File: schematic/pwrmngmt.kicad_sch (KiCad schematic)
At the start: 46 parts, among them U10 BSD316, U11 BSD316, U12 PC817, U13 PC817, U14 PC817, U15 AS431, U16 LM324, U17 XL6009, U18 PAM2305CGFADJ, U9 BSD316

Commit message: a
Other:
- title: (none) -> Power Managment
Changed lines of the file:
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@@
 (kicad_sch (version 20211123) (generator eeschema)
   (paper "A4")
+  (title_block
+    (title "Power Managment")
+    (date "2022-03-18")
+    (comment 1 "Engineer/Draftsman: Joesphan Lu")
+  )
   (junction (at 251.46 24.13) (diameter 0) (color 0 0 0 0)
   )

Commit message: e
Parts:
- removed C16: 100uF, Capacitor_SMD:C_1210_3225Metric_Pad1.33x2.70mm_HandSolder, symbol Device:C
- removed C17: 10uF, Capacitor_SMD:C_0805_2012Metric_Pad1.18x1.45mm_HandSolder, symbol Device:C
- removed C18: 1uF, Capacitor_SMD:C_0805_2012Metric_Pad1.18x1.45mm_HandSolder, symbol Device:C
- removed C20: Cfw (DNP), Capacitor_SMD:C_0805_2012Metric_Pad1.18x1.45mm_HandSolder, symbol Device:C
- removed L2: 10uH NR8040T100M, Inductor_SMD:L_Taiyo-Yuden_NR-80xx_HandSoldering, symbol Device:L
- removed R13: 33k, Resistor_SMD:R_0805_2012Metric_Pad1.20x1.40mm_HandSolder, symbol Device:R
- removed R14: 7.5k, Resistor_SMD:R_0805_2012Metric_Pad1.20x1.40mm_HandSolder, symbol Device:R
- removed R35, R36: 1k, Resistor_SMD:R_0805_2012Metric_Pad1.20x1.40mm_HandSolder, symbol Device:R
- removed R37, R38: 12.5k, Resistor_SMD:R_0805_2012Metric_Pad1.20x1.40mm_HandSolder, symbol Device:R
- removed unit 1 of U16
- removed U18: PAM2305CGFADJ, Package_DFN_QFN:DFN-6-1EP_2x2mm_P0.65mm_EP1x1.6mm, symbol Regulator_Switching:PAM2305CGFADJ
- added C?: 100nF, Capacitor_SMD:C_0805_2012Metric_Pad1.18x1.45mm_HandSolder, symbol Device:C
- added C?: 84nF, Capacitor_SMD:C_0805_2012Metric_Pad1.18x1.45mm_HandSolder, symbol Device:C
- added C? (x2): 1uF, Capacitor_SMD:C_0805_2012Metric_Pad1.18x1.45mm_HandSolder, symbol Device:C
- added C?: 10uF, Capacitor_SMD:C_0805_2012Metric_Pad1.18x1.45mm_HandSolder, symbol Device:C
- added C?: 100uF, Capacitor_SMD:C_1210_3225Metric_Pad1.33x2.70mm_HandSolder, symbol Device:C
- added L?: 33uH, Inductor_SMD:L_10.4x10.4_H4.8, symbol Device:L
- added R4: .1, Resistor_SMD:R_1206_3216Metric_Pad1.30x1.75mm_HandSolder, symbol Device:R
- added R5, R6: 1k, Resistor_SMD:R_0805_2012Metric_Pad1.20x1.40mm_HandSolder, symbol Device:R
- added R7: 12.5k, Resistor_SMD:R_0805_2012Metric_Pad1.20x1.40mm_HandSolder, symbol Device:R
- added R? (x2): 50k, Resistor_SMD:R_0805_2012Metric_Pad1.20x1.40mm_HandSolder, symbol Device:R
- added R?: 3k, Resistor_SMD:R_0805_2012Metric_Pad1.20x1.40mm_HandSolder, symbol Device:R
- added R?: 39k, Resistor_SMD:R_0805_2012Metric_Pad1.20x1.40mm_HandSolder, symbol Device:R
- added R?: 7.5k, Resistor_SMD:R_0805_2012Metric_Pad1.20x1.40mm_HandSolder, symbol Device:R
- added R?: 33k, Resistor_SMD:R_0805_2012Metric_Pad1.20x1.40mm_HandSolder, symbol Device:R
- added U5: LM324, Package_SO:SOIC-14_3.9x8.7mm_P1.27mm, symbol Amplifier_Operational:LM324
- added U?: AOZ6662DI, 1KicadLib:DFN_8_3x3mm_EP_1.25x2.7mm, symbol 1KicadLib:AOZ6662DI
- added U?: AS431, Package_TO_SOT_SMD:SOT-23_Handsoldering, symbol 1KicadLib:AS431
- D4: footprint Diode_SMD:D_SMC_Handsoldering -> Diode_SMD:D_SMA_Handsoldering
- L3: footprint Inductor_SMD:L_12x12mm_H4.5mm -> Inductor_SMD:L_10.4x10.4_H4.8
- R34: value .1 -> 12.5k; footprint Resistor_SMD:R_1206_3216Metric_Pad1.30x1.75mm_HandSolder -> Resistor_SMD:R_0805_2012Metric_Pad1.20x1.40mm_HandSolder
- U12, U13, U14: footprint Package_SO:SOP-4_3.8x4.1mm_P2.54mm -> Package_DIP:DIP-4_W7.62mm
- U15: footprint Package_TO_SOT_SMD:SOT-23-5_HandSoldering -> Package_TO_SOT_SMD:SOT-23_Handsoldering
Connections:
- net +3V3: now also C?.1, C?.1, C?.1, L?.2, R?.1
- net +BATT: now also R?.2
- net GND: now also U17.1 (GND), C?.2, C?.2, C?.2, C?.2, C?.2, R4.1, R6.2, R7.2, R?.2, U?.1 (GND), U?.9 (EP/GND); no longer BT3.2 (-), R34.2, U11.4 (S)
- net at R34.1: now also R6.1, U5.3 (+); no longer U17.1 (GND)
- net at U17.5 (FB): now also R34.2, U5.1
- new net: BT3.2 (-), R4.2, R5.2, U11.4 (S)
- new net: C?.1, U?.8 (BOOTSTRP)
- new net: C?.2, L?.1, U?.2 (LX/SW)
- new net: R?.1, R?.2, U?.1
- new net: R?.2, U?.4 (COMP)
- new net: C?.1, U?.5 (VCC)
- new net: R?.1, R?.2, U?.6 (FB)
- new net: C?.1, R?.1
- new net: R5.1, R7.1, U5.2 (-)
- new net: R?.1, U?.3
- new net +5V: R?.1, R?.2, U?.2
- new net PWR_UNSW: U?.3 (VIN), U?.7 (EN)
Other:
- note added: "2.25V off each divider = 4.1V on the battery"
- note added: "3.3V Buck"
- note added: "5V Low Current"
- note added: "Battery Balancing"
- note added: "Constant Current Battery Charging"
- note added: "Current detection"
- note added: "Sheet Ports"
- note added: "Voltage Detection Vbatmax = 4.1V"
- note removed: "2.5V on the voltage divider is about 4.1 V per cell disables the XL6009 when it reaches"
- note removed: "Battery balancing, do it in software 2.25V = 4.1V"
- moved on the sheet: BT1, BT2, BT3, C15, C21, D4, L3, R12, R15, R16, R17, R18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

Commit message: d
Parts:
- removed R? (x2): 50k, Resistor_SMD:R_0805_2012Metric_Pad1.20x1.40mm_HandSolder, symbol Device:R
- removed R?: 3k, Resistor_SMD:R_0805_2012Metric_Pad1.20x1.40mm_HandSolder, symbol Device:R
- removed U?: AS431, Package_TO_SOT_SMD:SOT-23_Handsoldering, symbol 1KicadLib:AS431
- added C11, C13, C16, C18, C20, C23: (no value), symbol Device:C
- added L4: (no value), symbol Device:L
- added R11: 15k, symbol Device:R
- added R14: 110k, symbol Device:R
- added R3: (no value), symbol Device:R
- added U20: (no value), 1KicadLib:DFN_8_3x3mm_EP_1.25x2.7mm, symbol 1KicadLib:AOZ6662DI
- BT1, BT2, BT3: value Battery_Cell -> (none); footprint Connector_PinHeader_2.54mm:PinHeader_1x02_P2.54mm_Vertical -> (none)
- C12, C22: renamed from C?; value 1uF -> (none); footprint Capacitor_SMD:C_0805_2012Metric_Pad1.18x1.45mm_HandSolder -> (none)
- C14: renamed from C?; value 100nF -> (none); footprint Capacitor_SMD:C_0805_2012Metric_Pad1.18x1.45mm_HandSolder -> (none)
- C15: value 10uF -> (none); footprint Capacitor_SMD:C_0805_2012Metric_Pad1.18x1.45mm_HandSolder -> (none)
- C17: renamed from C?; value 100uF -> (none); footprint Capacitor_SMD:C_1210_3225Metric_Pad1.33x2.70mm_HandSolder -> (none)
- C19: renamed from C?; value 10uF -> (none); footprint Capacitor_SMD:C_0805_2012Metric_Pad1.18x1.45mm_HandSolder -> (none)
- C21: value 100nF -> (none); footprint Capacitor_SMD:C_0805_2012Metric_Pad1.18x1.45mm_HandSolder -> (none)
- C9: renamed from C?; value 84nF -> (none); footprint Capacitor_SMD:C_0805_2012Metric_Pad1.18x1.45mm_HandSolder -> (none)
- D4: value SS34 -> (none); footprint Diode_SMD:D_SMA_Handsoldering -> (none)
- L2: renamed from L?; value 33uH -> (none); footprint Inductor_SMD:L_10.4x10.4_H4.8 -> (none)
- L3: value 33uH -> (none); footprint Inductor_SMD:L_10.4x10.4_H4.8 -> (none)
- R10: renamed from R?; value 7.5k -> (none); footprint Resistor_SMD:R_0805_2012Metric_Pad1.20x1.40mm_HandSolder -> (none)
- R12, R15, R16: value 28.7 -> (none); footprint Resistor_SMD:R_2512_6332Metric_Pad1.40x3.35mm_HandSolder -> (none)
- R13: renamed from R?; value 33k -> (none); footprint Resistor_SMD:R_0805_2012Metric_Pad1.20x1.40mm_HandSolder -> (none)
- R17, R18, R19: value 200 -> (none); footprint Resistor_SMD:R_0805_2012Metric_Pad1.20x1.40mm_HandSolder -> (none)
- R2: renamed from R?; value 39k -> (none); footprint Resistor_SMD:R_0805_2012Metric_Pad1.20x1.40mm_HandSolder -> (none)
- R22: value 100k -> (none); footprint Resistor_SMD:R_0805_2012Metric_Pad1.20x1.40mm_HandSolder -> (none)
- R23: value 22k -> (none); footprint Resistor_SMD:R_0805_2012Metric_Pad1.20x1.40mm_HandSolder -> (none)
- R25: value 390 -> (none); footprint Resistor_SMD:R_0805_2012Metric_Pad1.20x1.40mm_HandSolder -> (none)
- R26: value 180k -> (none); footprint Resistor_SMD:R_0805_2012Metric_Pad1.20x1.40mm_HandSolder -> (none)
- R27, R29: value 68k -> (none); footprint Resistor_SMD:R_0805_2012Metric_Pad1.20x1.40mm_HandSolder -> (none)
- R28, R31: value 56k -> (none); footprint Resistor_SMD:R_0805_2012Metric_Pad1.20x1.40mm_HandSolder -> (none)
- R30: value 220k -> (none); footprint Resistor_SMD:R_0805_2012Metric_Pad1.20x1.40mm_HandSolder -> (none)
- R32: value 120 -> (none); footprint Resistor_SMD:R_0805_2012Metric_Pad1.20x1.40mm_HandSolder -> (none)
- R33: value 500 -> (none); footprint Resistor_SMD:R_0805_2012Metric_Pad1.20x1.40mm_HandSolder -> (none)
- R34, R7: value 12.5k -> (none); footprint Resistor_SMD:R_0805_2012Metric_Pad1.20x1.40mm_HandSolder -> (none)
- R4: value .1 -> (none); footprint Resistor_SMD:R_1206_3216Metric_Pad1.30x1.75mm_HandSolder -> (none)
- R5, R6: value 1k -> (none); footprint Resistor_SMD:R_0805_2012Metric_Pad1.20x1.40mm_HandSolder -> (none)
- U10, U11, U9: value BSD316 -> (none)
- U12, U13, U14: value PC817 -> (none)
- U15: value AS431 -> (none); footprint Package_TO_SOT_SMD:SOT-23_Handsoldering -> Package_TO_SOT_SMD:SOT-23-5_HandSoldering
- U16, U5: value LM324 -> (none); footprint Package_SO:SOIC-14_3.9x8.7mm_P1.27mm -> (none)
- U17: value XL6009 -> (none); footprint Package_TO_SOT_SMD:TO-263-5_TabPin3 -> (none)
- U19: renamed from U?; value AOZ6662DI -> (none)
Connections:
- net +5V: now also C18.1, C20.1, C23.1, L4.2, R14.1
- net GND: now also C11.2, C13.2, C18.2, C20.2, C23.2, R11.2, U20.1 (GND), U20.9 (EP/GND)
- net PWR_UNSW: now also U20.3 (VIN), U20.7 (EN)
- new net: R11.1, R14.2, U20.6 (FB)
- new net: C13.1, U20.5 (VCC)
- new net: C16.1, U20.8 (BOOTSTRP)
- new net: C16.2, L4.1, U20.2 (LX/SW)
- new net: C11.1, R3.1
- new net: R3.2, U20.4 (COMP)
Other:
- note added: "5V Buck"
- note removed: "5V Low Current"

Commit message: d
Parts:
- removed C17, C18: (no value), symbol Device:C
- removed R32: (no value), symbol Device:R
- BT1, BT2, BT3: value (none) -> Battery_Cell; footprint (none) -> Connector_PinHeader_2.54mm:PinHeader_1x02_P2.54mm_Vertical
- C11, C9: value (none) -> 84nF; footprint (none) -> Capacitor_SMD:C_0805_2012Metric_Pad1.18x1.45mm_HandSolder
- C12, C13, C22, C23: value (none) -> 1uF; footprint (none) -> Capacitor_SMD:C_0805_2012Metric_Pad1.18x1.45mm_HandSolder
- C14, C16, C21: value (none) -> 100nF; footprint (none) -> Capacitor_SMD:C_0805_2012Metric_Pad1.18x1.45mm_HandSolder
- C15, C19, C20: value (none) -> 10uF; footprint (none) -> Capacitor_SMD:C_0805_2012Metric_Pad1.18x1.45mm_HandSolder
- D4: value (none) -> SS34; footprint (none) -> Diode_SMD:D_SMA_Handsoldering
- L2, L3, L4: value (none) -> 33uH; footprint (none) -> Inductor_SMD:L_10.4x10.4_H4.8
- R10: value (none) -> 7.5k; footprint (none) -> Resistor_SMD:R_0805_2012Metric_Pad1.20x1.40mm_HandSolder
- R11, R14: footprint (none) -> Resistor_SMD:R_0805_2012Metric_Pad1.20x1.40mm_HandSolder
- R12, R15, R16: value (none) -> 28.7; footprint (none) -> Resistor_SMD:R_2512_6332Metric_Pad1.40x3.35mm_HandSolder
- R13: value (none) -> 33k; footprint (none) -> Resistor_SMD:R_0805_2012Metric_Pad1.20x1.40mm_HandSolder
- R17, R18, R19: value (none) -> 200; footprint (none) -> Resistor_SMD:R_0805_2012Metric_Pad1.20x1.40mm_HandSolder
- R2, R3: value (none) -> 39k; footprint (none) -> Resistor_SMD:R_0805_2012Metric_Pad1.20x1.40mm_HandSolder
- R22, R26: value (none) -> 180k; footprint (none) -> Resistor_SMD:R_0805_2012Metric_Pad1.20x1.40mm_HandSolder
- R23: value (none) -> 36k; footprint (none) -> Resistor_SMD:R_0805_2012Metric_Pad1.20x1.40mm_HandSolder
- R25: value (none) -> 4.3k; footprint (none) -> Resistor_SMD:R_0805_2012Metric_Pad1.20x1.40mm_HandSolder
- R27: value (none) -> 68k; footprint (none) -> Resistor_SMD:R_0805_2012Metric_Pad1.20x1.40mm_HandSolder
- R28: value (none) -> 510k; footprint (none) -> Resistor_SMD:R_0805_2012Metric_Pad1.20x1.40mm_HandSolder
- R29: value (none) -> 620k; footprint (none) -> Resistor_SMD:R_0805_2012Metric_Pad1.20x1.40mm_HandSolder
- R30: value (none) -> 200k; footprint (none) -> Resistor_SMD:R_0805_2012Metric_Pad1.20x1.40mm_HandSolder
- R31: value (none) -> 51k; footprint (none) -> Resistor_SMD:R_0805_2012Metric_Pad1.20x1.40mm_HandSolder
- R33: value (none) -> 500; footprint (none) -> Resistor_SMD:R_0805_2012Metric_Pad1.20x1.40mm_HandSolder
- R34, R7: value (none) -> 12.5k; footprint (none) -> Resistor_SMD:R_0805_2012Metric_Pad1.20x1.40mm_HandSolder
- R4: value (none) -> .1; footprint (none) -> Resistor_SMD:R_1206_3216Metric_Pad1.30x1.75mm_HandSolder
- R5, R6: value (none) -> 1k; footprint (none) -> Resistor_SMD:R_0805_2012Metric_Pad1.20x1.40mm_HandSolder
- U10, U11, U9: value (none) -> BSD316
- U12, U13, U14: value (none) -> PC817
- U15: value (none) -> AS431
- U17: value (none) -> XL6009; footprint (none) -> Package_TO_SOT_SMD:TO-263-5_TabPin3
- U19, U20: value (none) -> AOZ6662DI
- U5: renamed from U16; value (none) -> LM324; footprint (none) -> Package_SO:SOIC-14_3.9x8.7mm_P1.27mm
- U5: value (none) -> LM324; footprint (none) -> Package_SO:SOIC-14_3.9x8.7mm_P1.27mm
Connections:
- net GND: now also R31.2
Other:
- moved on the sheet: C19, C20, C22, C23

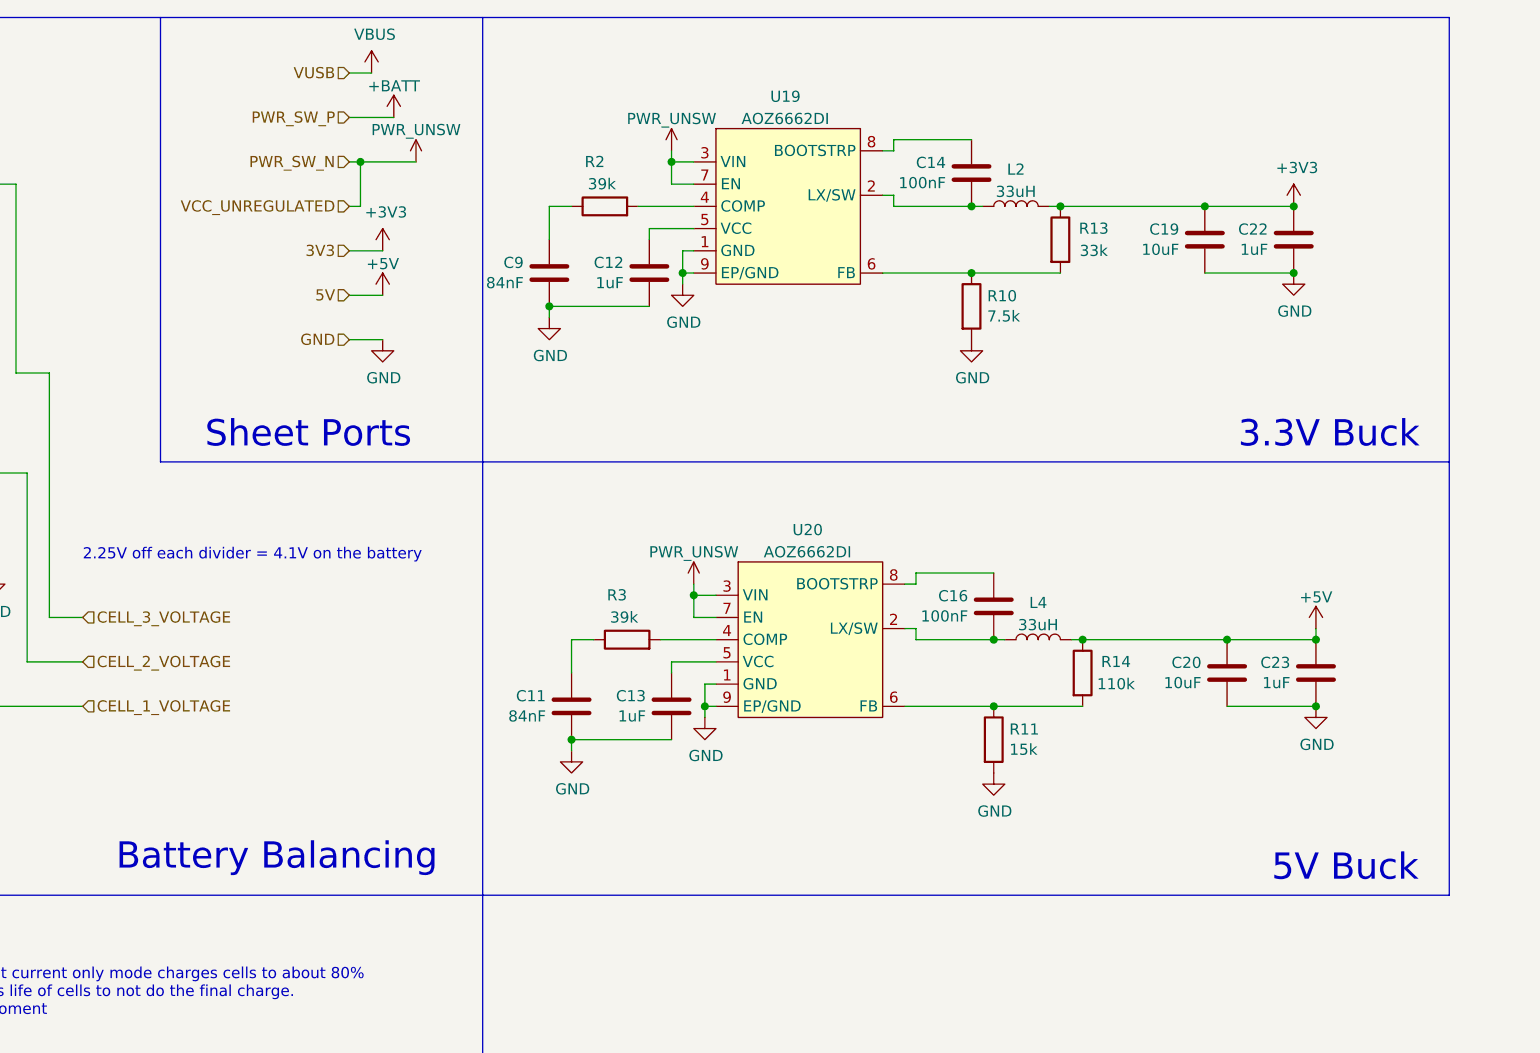
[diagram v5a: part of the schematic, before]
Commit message: beta boards routed
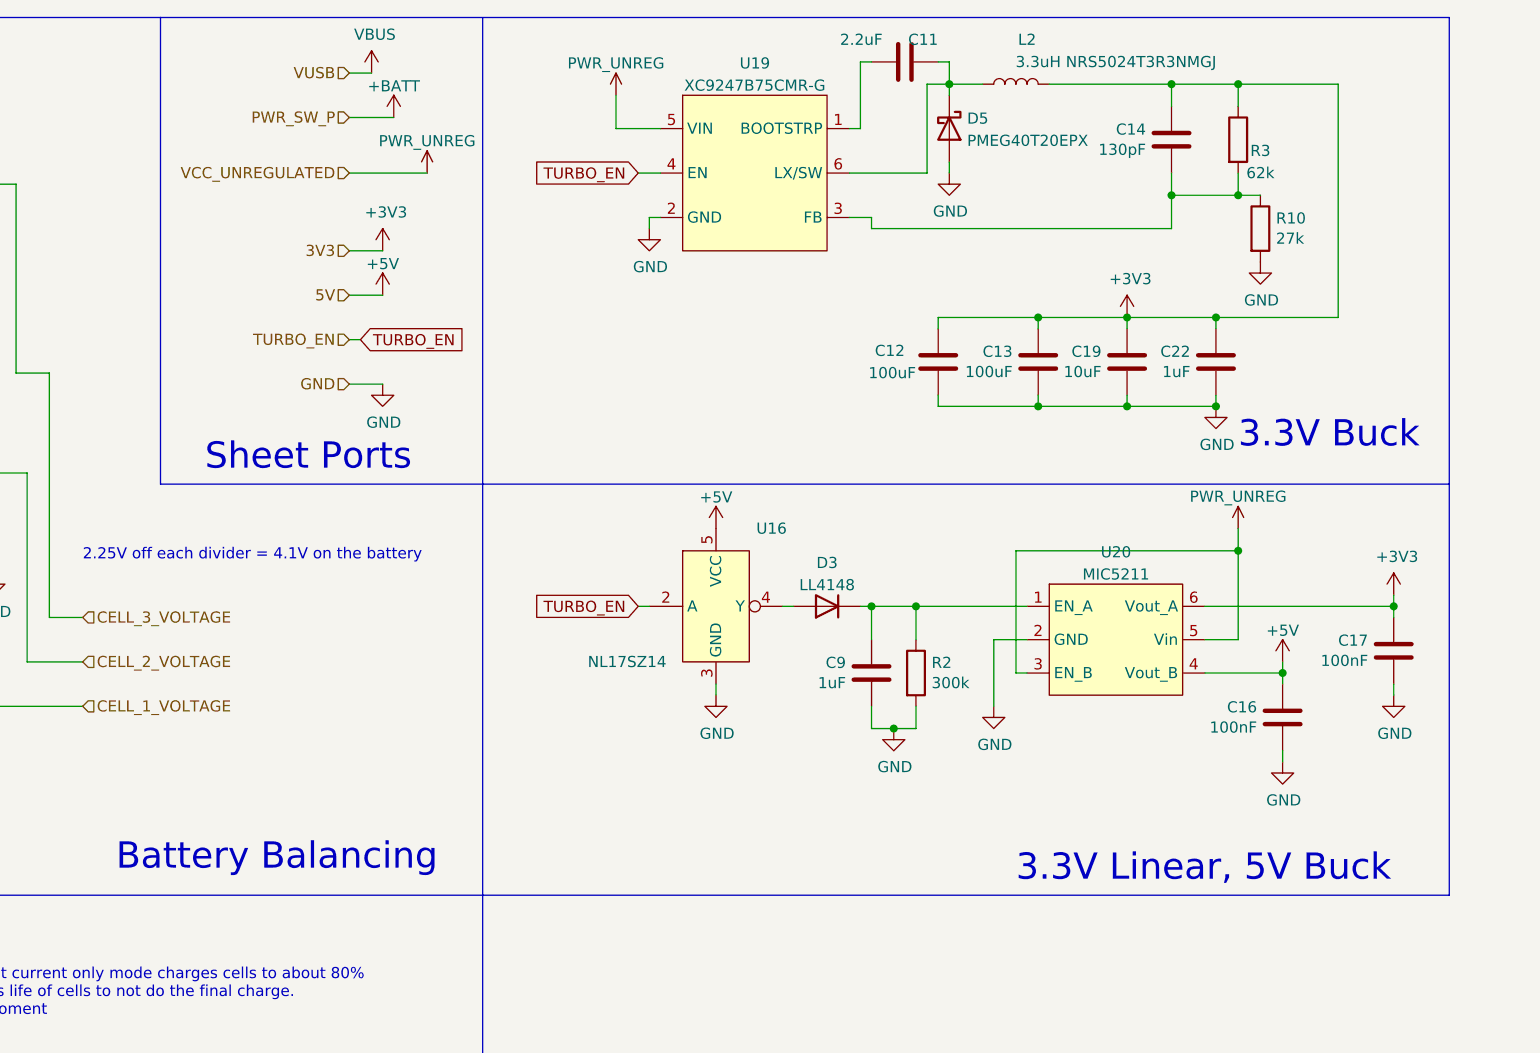
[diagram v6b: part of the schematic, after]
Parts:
- removed C20: 10uF, Capacitor_SMD:C_0805_2012Metric_Pad1.18x1.45mm_HandSolder, symbol Device:C
- removed C23: 1uF, Capacitor_SMD:C_0805_2012Metric_Pad1.18x1.45mm_HandSolder, symbol Device:C
- removed L4: 33uH, Inductor_SMD:L_10.4x10.4_H4.8, symbol Device:L
- removed R11: 15k, Resistor_SMD:R_0805_2012Metric_Pad1.20x1.40mm_HandSolder, symbol Device:R
- removed R13: 33k, Resistor_SMD:R_0805_2012Metric_Pad1.20x1.40mm_HandSolder, symbol Device:R
- removed R14: 110k, Resistor_SMD:R_0805_2012Metric_Pad1.20x1.40mm_HandSolder, symbol Device:R
- removed U19, U20: AOZ6662DI, 1KicadLib:DFN_8_3x3mm_EP_1.25x2.7mm, symbol 1KicadLib:AOZ6662DI
- added C17: 100nF, Capacitor_SMD:C_0805_2012Metric_Pad1.18x1.45mm_HandSolder, symbol Device:C
- added D3: LL4148, Diode_SMD:D_MiniMELF, symbol Diode:LL4148
- added D5: PMEG40T20EPX, Diode_SMD:D_SOD-128, symbol Device:D_Schottky
- added U16: NL17SZ14, Package_TO_SOT_SMD:SOT-553, symbol 1KicadLib:NL17SZ14
- added U19: XC9247B75CMR-G, Package_TO_SOT_SMD:SOT-23-6_Handsoldering, symbol 1KicadLib:XC9247B75CMR-G
- added U20: MIC5211, Package_TO_SOT_SMD:SOT-23-6_Handsoldering, symbol 1KicadLib:MIC5211
- C11: value 84nF -> 2.2uF
- C12, C13: value 1uF -> 100uF; footprint Capacitor_SMD:C_0805_2012Metric_Pad1.18x1.45mm_HandSolder -> Capacitor_SMD:C_1210_3225Metric_Pad1.33x2.70mm_HandSolder
- C14: value 100nF -> 130pF
- C9: value 84nF -> 1uF
- L2: value 33uH -> 3.3uH NRS5024T3R3NMGJ; footprint Inductor_SMD:L_10.4x10.4_H4.8 -> Inductor_SMD:L_Taiyo-Yuden_NR-50xx_HandSoldering
- R10: value 7.5k -> 27k
- R2: value 39k -> 300k
- R3: value 39k -> 62k
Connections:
- net +3V3: now also C12.1, C13.1, C14.1, R3.1, C17.1, U20.6 (Vout_A)
- net +5V: now also C16.1, U16.5 (VCC), U20.4 (Vout_B)
- net GND: now also C16.2, R2.2, C17.2, D5.2 (A), U16.3 (GND), U19.2 (GND), U20.2 (GND); no longer C11.2
- net at C14.2: now also R10.1, R3.2, U19.3 (FB); no longer L2.1
- net at C9.1, R2.1: now also D3.1 (K), U20.1 (EN_A)
- net at C11.1: now also U19.1 (BOOTSTRP); no longer R3.1
- new net: C11.2, D5.1 (K), L2.1, U19.6 (LX/SW)
- new net: D3.2 (A), U16.4 (Y)
- new net PWR_UNREG: U19.5 (VIN), U20.3 (EN_B), U20.5 (Vin)
- new net TURBO_EN: U16.2 (A), U19.4 (EN)
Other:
- note added: "3.3V Linear, 5V Buck"
- note removed: "5V Buck"
- moved on the sheet: C19, C22

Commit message: prelim ble working
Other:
- note added: "3.3V Linear, 5V Linear"
- note removed: "3.3V Linear, 5V Buck"
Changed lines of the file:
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@@
     (effects (font (size 1.27 1.27)) (justify left bottom))
   )
-  (text "3.3V Linear, 5V Buck" (at 232.41 113.03 0)
+  (text "3.3V Linear, 5V Linear" (at 232.41 113.03 0)
     (effects (font (size 3 3)) (justify left bottom))
   )
